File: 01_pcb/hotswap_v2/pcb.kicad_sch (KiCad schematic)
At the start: 131 parts, among them J1 TYPE-C-31-M12_13, J2 AVR-ISP-6_mod, J3 Conn_01x01, J4 Conn_01x01, J5 Conn_01x01, J6 Conn_01x01, J7 Conn_01x01, K1 KEYSW, K10 KEYSW, K11 KEYSW, K12 KEYSW, K13 KEYSW, K14 KEYSW, K15 KEYSW, K16 KEYSW, K17 KEYSW, K18 KEYSW, K19 KEYSW, K2 KEYSW, K20 KEYSW, K21 KEYSW, K22 KEYSW, K23 KEYSW, K24 KEYSW, K25 KEYSW, K26 KEYSW, K27 KEYSW, K28 KEYSW, K29 KEYSW, K3 KEYSW, K30 KEYSW, K31 KEYSW, K32 KEYSW, K33 KEYSW, K34 KEYSW, K35 KEYSW, K36 KEYSW, K37 KEYSW, K38 KEYSW, K39 KEYSW, K4 KEYSW, K40 KEYSW, K41 KEYSW, K42 KEYSW, K43 KEYSW, K44 KEYSW, K45 KEYSW, K46 KEYSW, K47 KEYSW, K48 KEYSW, K5 KEYSW, K50 KEYSW, K51 KEYSW, K52 KEYSW, K6 KEYSW, K7 KEYSW, K8 KEYSW, K9 KEYSW, SW1 SW_PUSH, SW2 Rotary_Encoder_Switch, U1 ATMEGA32U4, U2 PRTR5V0U2X, Y1 16MHz

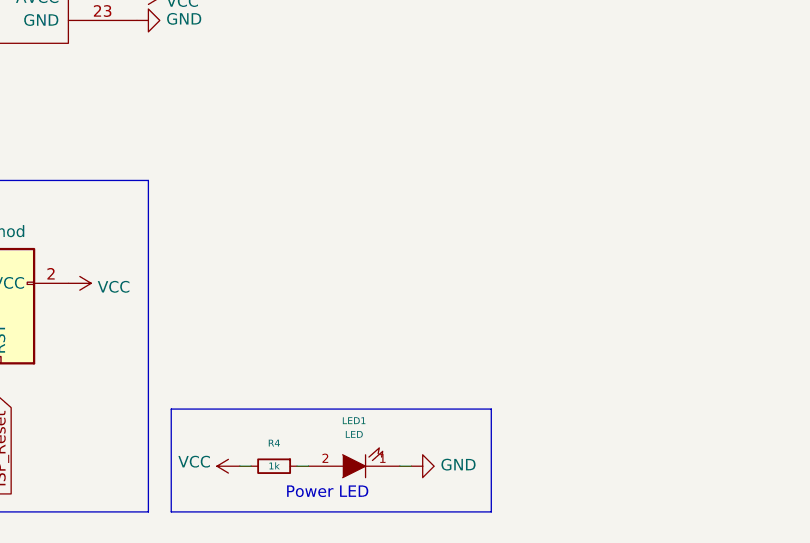
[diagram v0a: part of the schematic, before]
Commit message: add mounting support for encoder
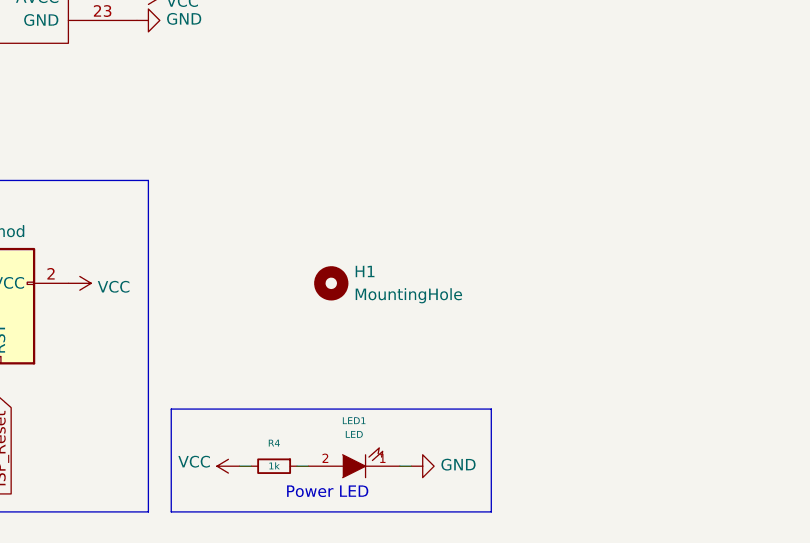
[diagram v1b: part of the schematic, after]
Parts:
- added H1: MountingHole, MountingHole:MountingHole_2.2mm_M2_DIN965_Pad, symbol Mechanical:MountingHole
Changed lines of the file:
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@@
     (pin "1")
+  )
+  (symbol (lib_id "Mechanical:MountingHole") (at 210.82 217.17 0) (unit 1)
+    (in_bom yes) (on_board yes) (fields_autoplaced)
+    (property "Reference" "H1" (id 0) (at 213.36 215.8999 0)
+      (effects (font (size 1.27 1.27)) (justify left))
+    )
+    (property "Value" "MountingHole" (id 1) (at 213.36 218.4399 0)
+      (effects (font (size 1.27 1.27)) (justify left))
+    )
+    (property "Footprint" "MountingHole:MountingHole_2.2mm_M2_DIN965_Pad" (id 2) (at 210.82 217.17 0)
+      (effects (font (size 1.27 1.27)) hide)
+    )
+    (property "Datasheet" "~" (id 3) (at 210.82 217.17 0)
+      (effects (font (size 1.27 1.27)) hide)
+    )
   )
   (symbol (lib_id "Connector_Generic:Conn_01x01") (at 129.54 187.96 180) (unit 1)
@@
       (reference "F1") (unit 1) (value ".5A") (footprint "Fuse:Fuse_0805_2012Metric_Pad1.15x1.40mm_HandSolder")
     )
+    (path "/1460489b-8b5f-418d-9774-df0d764bc56a"
+      (reference "H1") (unit 1) (value "MountingHole") (footprint "MountingHole:MountingHole_2.2mm_M2_DIN965_Pad")
+    )
     (path "/00000000-0000-0000-0000-00005e315a49"
